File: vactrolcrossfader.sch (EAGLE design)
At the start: 60 parts, among them U1 TL072_SMD

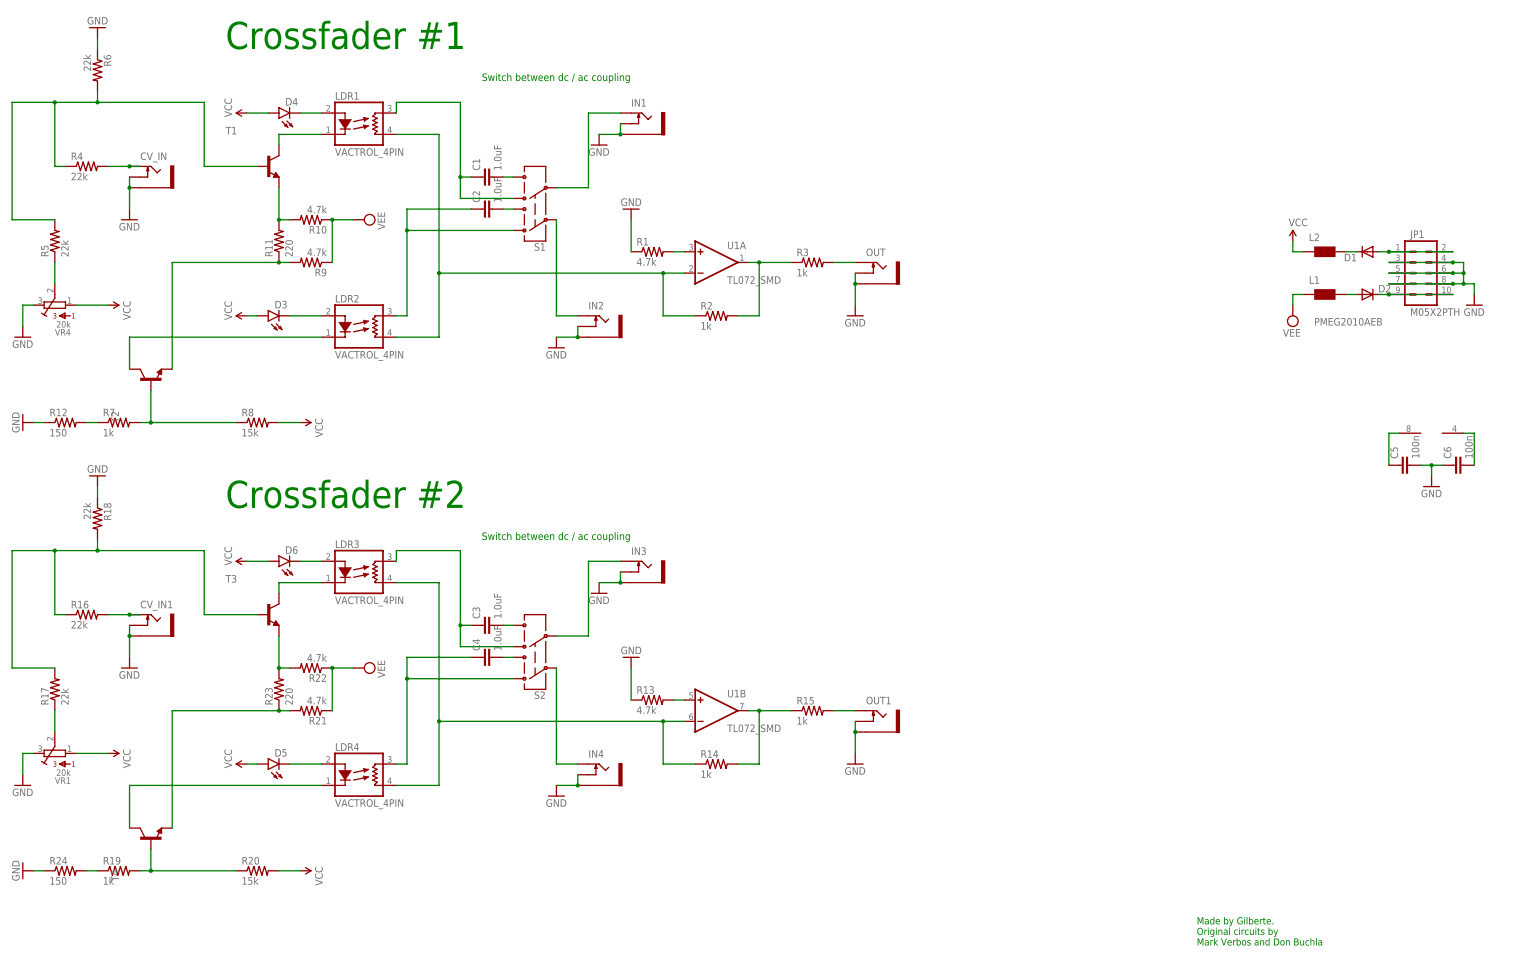
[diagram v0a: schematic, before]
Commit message: Added switch to CV inputs
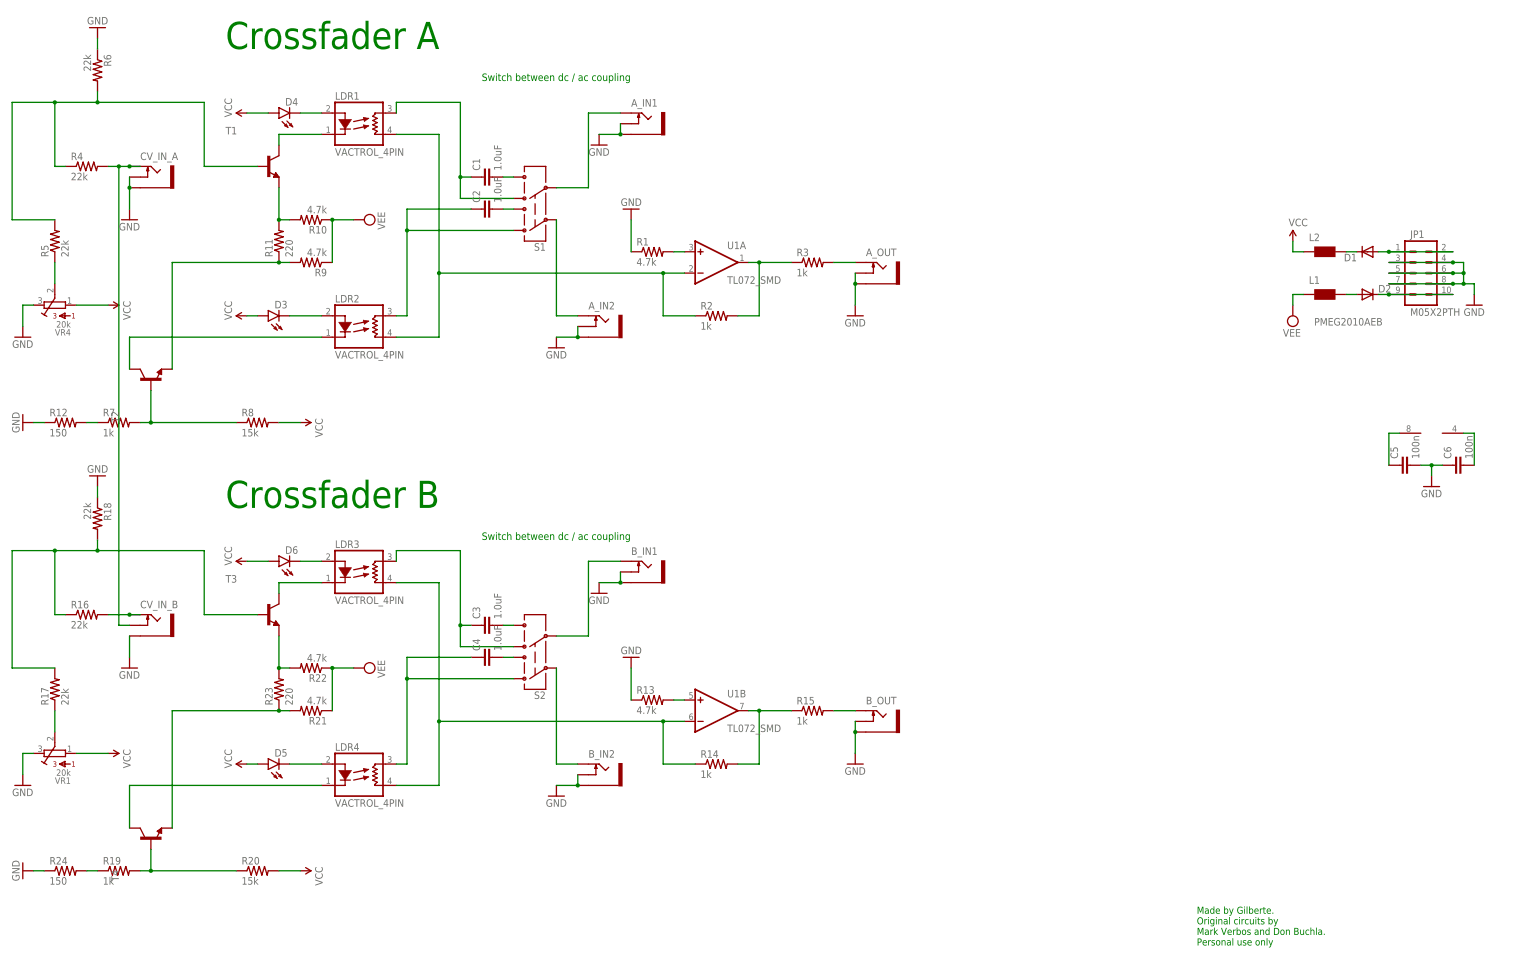
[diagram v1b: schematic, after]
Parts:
- renumbered CV_IN to CV_IN_A, CV_IN1 to CV_IN_B, IN1 to A_IN1, IN2 to A_IN2, IN3 to B_IN1, IN4 to B_IN2, OUT to A_OUT, OUT1 to B_OUT
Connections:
- net GND: no longer CV_IN_B.SWITCH
- net N$11: now also CV_IN_B.SWITCH
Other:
- note added: "Crossfader A"
- note added: "Crossfader B"
- note added: "Made by Gilberte. Original circuits by Mark Verbos and Don Buchla. Personal use only"
- note removed: "Crossfader #1"
- note removed: "Crossfader #2"
- note removed: "Made by Gilberte. Original circuits by Mark Verbos and Don Buchla"

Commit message: First board layout done
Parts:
- removed C1, C2: 1.0uF, SparkFun-Capacitors:1.0UF-25V-+80/-20(0805)"
- removed D1, D2: PMEG2010AEB, diode:DIODE-SOD523
- removed JP1: M05X2PTH, og-header:M05X2PTH
- removed L1, L2: (no value), wuerth-elektronik:WE-CBF_0603
- removed S1, S2: (no value), SparkFun-Electromechanical:SWITCH-DPDTPTH1
- added C25, C30: 47u, rcl:CPOL-USD
- added D7, D8: 1N5819HW, diode:DIODE-SOD123
- added JP2: M05X2PTH, og-header:M05X2PTH
- C3, C4, C5, C6: device SparkFun-Capacitors:1.0UF-25V-+80/-20(0805)" -> SparkFun-Passives:CAP0805
- R1, R10, R11, R12, R13, R14, R15, R16, R17, R18, R19, R2, R20, R21, R22, R23, R24, R3, R4, R5, R6, R7, R8, R9: device SparkFun-Passives:RESISTOR0805-RES -> SparkFun-Passives:RESISTOR1206
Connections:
- removed net N$1: C1.2, S1.6
- removed net N$18: A_IN2.TIP, S1.2
- removed net N$20: D2.C, JP1.10, JP1.9
- removed net N$22: D1.C, L2.2
- removed net N$23: C1.1, LDR1.RES1, S1.4
- removed net N$24: C2.1, LDR2.RES1, S1.1
- removed net N$40: C3.2, S2.6
- removed net N$43: B_IN2.TIP, S2.2
- removed net N$44: D2.A, L1.2
- removed net N$6: D1.A, JP1.1, JP1.2
- new net N$56: D7.A, JP2.1, JP2.2
- new net N$64: D8.C, JP2.10, JP2.9
- net GND: now also C25.-, C30.+, JP2.3, JP2.4, JP2.5, JP2.6, JP2.7, JP2.8; no longer JP1.3, JP1.4, JP1.5, JP1.6, JP1.7, JP1.8
- net N$14: now also LDR1.RES1; no longer S1.5
- net N$2: now also A_IN2.TIP, LDR2.RES1; no longer C2.2, S1.3
- net N$41: now also B_IN2.TIP; no longer S2.3
- net N$42: now also C3.2; no longer S2.5
- net N$45: no longer S2.4
- net N$46: no longer S2.1
- net VCC: now also C25.+, D7.C; no longer L2.1
- net VEE: now also C30.-, D8.A; no longer L1.1
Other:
- note added: "AC Coupled"
- note added: "CV input of Crossfader A is automatically routed to the CV input of Crossfader B if no signal is present at the CV input of B"
- note added: "DC Coupled"
- note removed: "Switch between dc / ac coupling"
- moved on the sheet: A_IN2, B_IN1, C3, C4

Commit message: board done
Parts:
- JP2: value M05X2PTH -> EURO_POWER_HEADERFAT_PADS; device og-header:M05X2PTH -> MusicThingModular:EURO_POWER_HEADERFAT_PADS
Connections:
- net N$56: now also D8.C; no longer D7.A
- net N$64: now also D7.A; no longer D8.C
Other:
- moved on the sheet: JP2
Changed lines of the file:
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@@
 <part name="D7" library="diode" deviceset="DIODE-" device="SOD123" value="1N5819HW"/>
 <part name="D8" library="diode" deviceset="DIODE-" device="SOD123" value="1N5819HW"/>
-<part name="JP2" library="og-header" deviceset="M05X2" device="PTH"/>
+<part name="JP2" library="MusicThingModular" deviceset="EURO_POWER_HEADER" device="FAT_PADS"/>
 </parts>
 <sheets>
@@
 <instance part="C25" gate="G$1" x="312.42" y="137.16"/>
 <instance part="C30" gate="G$1" x="312.42" y="124.46"/>
-<instance part="GND19" gate="1" x="281.94" y="119.38"/>
+<instance part="GND19" gate="1" x="281.94" y="111.76"/>
 <instance part="P+10" gate="1" x="243.84" y="134.62"/>
 <instance part="SUPPLY4" gate="G$1" x="243.84" y="116.84" rot="R180"/>
@@
 </segment>
 <segment>
-<wire x1="274.32" y1="129.54" x2="274.32" y2="127" width="0.1524" layer="91"/>
 <wire x1="274.32" y1="127" x2="274.32" y2="124.46" width="0.1524" layer="91"/>
-<wire x1="256.54" y1="129.54" x2="271.78" y2="129.54" width="0.1524" layer="91"/>
-<wire x1="271.78" y1="129.54" x2="274.32" y2="129.54" width="0.1524" layer="91"/>
 <wire x1="274.32" y1="127" x2="271.78" y2="127" width="0.1524" layer="91"/>
-<wire x1="271.78" y1="127" x2="256.54" y2="127" width="0.1524" layer="91"/>
-<wire x1="256.54" y1="124.46" x2="271.78" y2="124.46" width="0.1524" layer="91"/>
-<wire x1="271.78" y1="124.46" x2="274.32" y2="124.46" width="0.1524" layer="91"/>
+<wire x1="256.54" y1="127" x2="271.78" y2="127" width="0.1524" layer="91"/>
 <wire x1="274.32" y1="124.46" x2="281.94" y2="124.46" width="0.1524" layer="91"/>
-<wire x1="281.94" y1="124.46" x2="281.94" y2="121.92" width="0.1524" layer="91"/>
-<junction x="274.32" y="127"/>
-<junction x="274.32" y="124.46"/>
+<wire x1="281.94" y1="124.46" x2="281.94" y2="114.3" width="0.1524" layer="91"/>
+<junction x="256.54" y="127"/>
+<junction x="271.78" y="127"/>
+<pinref part="GND19" gate="1" pin="GND"/>
+<pinref part="JP2" gate="G$1" pin="6"/>
+<pinref part="JP2" gate="G$1" pin="5"/>
 <junction x="271.78" y="124.46"/>
-<junction x="271.78" y="127"/>
+<pinref part="JP2" gate="G$1" pin="3"/>
+<wire x1="271.78" y1="124.46" x2="256.54" y2="124.46" width="0.1524" layer="91"/>
+<pinref part="JP2" gate="G$1" pin="4"/>
+<wire x1="271.78" y1="124.46" x2="271.78" y2="127" width="0.1524" layer="91"/>
+<pinref part="JP2" gate="G$1" pin="7"/>
+<wire x1="271.78" y1="129.54" x2="256.54" y2="129.54" width="0.1524" layer="91"/>
+<pinref part="JP2" gate="G$1" pin="8"/>
+<wire x1="271.78" y1="127" x2="271.78" y2="129.54" width="0.1524" layer="91"/>
 <junction x="271.78" y="129.54"/>
+<wire x1="256.54" y1="129.54" x2="256.54" y2="127" width="0.1524" layer="91"/>
 <junction x="256.54" y="129.54"/>
-<junction x="256.54" y="127"/>
+<wire x1="256.54" y1="127" x2="256.54" y2="124.46" width="0.1524" layer="91"/>
 <junction x="256.54" y="124.46"/>
-<pinref part="GND19" gate="1" pin="GND"/>
-<pinref part="JP2" gate="G$1" pin="8"/>
-<pinref part="JP2" gate="G$1" pin="6"/>
-<pinref part="JP2" gate="G$1" pin="4"/>
-<pinref part="JP2" gate="G$1" pin="7"/>
-<pinref part="JP2" gate="G$1" pin="5"/>
-<pinref part="JP2" gate="G$1" pin="3"/>
 </segment>
 <segment>
@@
 <net name="N$56" class="0">
 <segment>
-<wire x1="256.54" y1="132.08" x2="271.78" y2="132.08" width="0.1524" layer="91"/>
-<wire x1="254" y1="132.08" x2="256.54" y2="132.08" width="0.1524" layer="91"/>
-<junction x="256.54" y="132.08"/>
+<wire x1="271.78" y1="121.92" x2="256.54" y2="121.92" width="0.1524" layer="91"/>
 <pinref part="JP2" gate="G$1" pin="2"/>
 <pinref part="JP2" gate="G$1" pin="1"/>
-<pinref part="D7" gate="G$1" pin="A"/>
+<pinref part="D8" gate="G$1" pin="C"/>
+<wire x1="256.54" y1="121.92" x2="254" y2="121.92" width="0.1524" layer="91"/>
+<junction x="256.54" y="121.92"/>
 </segment>
 </net>
 <net name="N$64" class="0">
 <segment>
-<wire x1="256.54" y1="121.92" x2="271.78" y2="121.92" width="0.1524" layer="91"/>
-<wire x1="254" y1="121.92" x2="256.54" y2="121.92" width="0.1524" layer="91"/>
-<junction x="256.54" y="121.92"/>
+<wire x1="271.78" y1="132.08" x2="256.54" y2="132.08" width="0.1524" layer="91"/>
 <pinref part="JP2" gate="G$1" pin="10"/>
 <pinref part="JP2" gate="G$1" pin="9"/>
-<pinref part="D8" gate="G$1" pin="C"/>
-</segment>
-</net>
+<pinref part="D7" gate="G$1" pin="A"/>
+<wire x1="256.54" y1="132.08" x2="254" y2="132.08" width="0.1524" layer="91"/>
+<junction x="256.54" y="132.08"/>
+</segment>
+</net>

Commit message: v1.2 first commit
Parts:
- removed VR1, VR4: 20k, MusicThingModular:BOURNS_3362P_TRIMMERP
- added VR2, VR3: 25k, MusicThingModular:9MM_SNAP-IN_POT_
- D3, D4, D5, D6: value (none) -> 3mm led
- R14, R2: value 1k -> 10k
- T1, T2, T3, T4: value (none) -> mmbt3904
- U1: value TL072_SMD -> TL072D; device MusicThingModular:TL072_SMD -> linear:TL072D
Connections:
- removed net N$47: C5.1, U1P.V+
- removed net N$48: C6.2, U1P.V-
- net GND: now also C5.1, VR2.E, VR3.E; no longer C5.2, VR1.3, VR4.3
- net N$13: now also VR3.S; no longer VR4.2
- net N$33: now also VR2.S; no longer VR1.2
- net VCC: now also C5.2, U1P.V+, VR2.A, VR3.A; no longer VR1.1, VR4.1
- net VEE: now also C6.2, U1P.V-
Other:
- moved on the sheet: B_IN1, C5, C6
